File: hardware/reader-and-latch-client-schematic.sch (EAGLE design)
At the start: 23 parts, among them IC1 MAX3468ESA, IC2 L272M, T1 TIP32

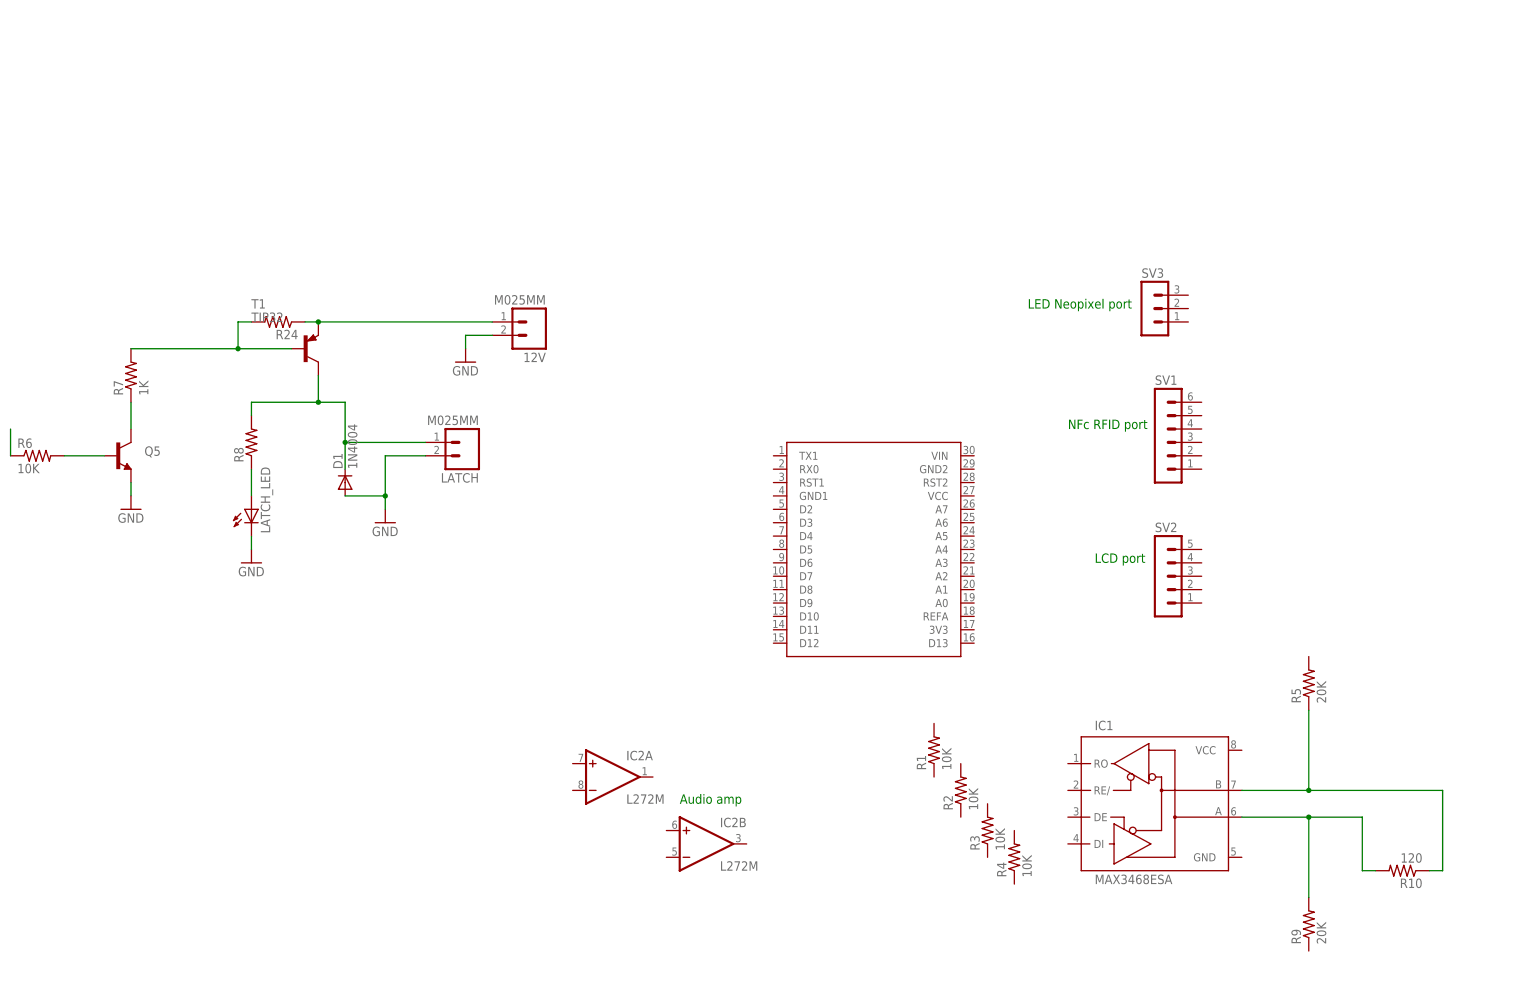
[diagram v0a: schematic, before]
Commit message: Add Tom's 13-2015 schematic
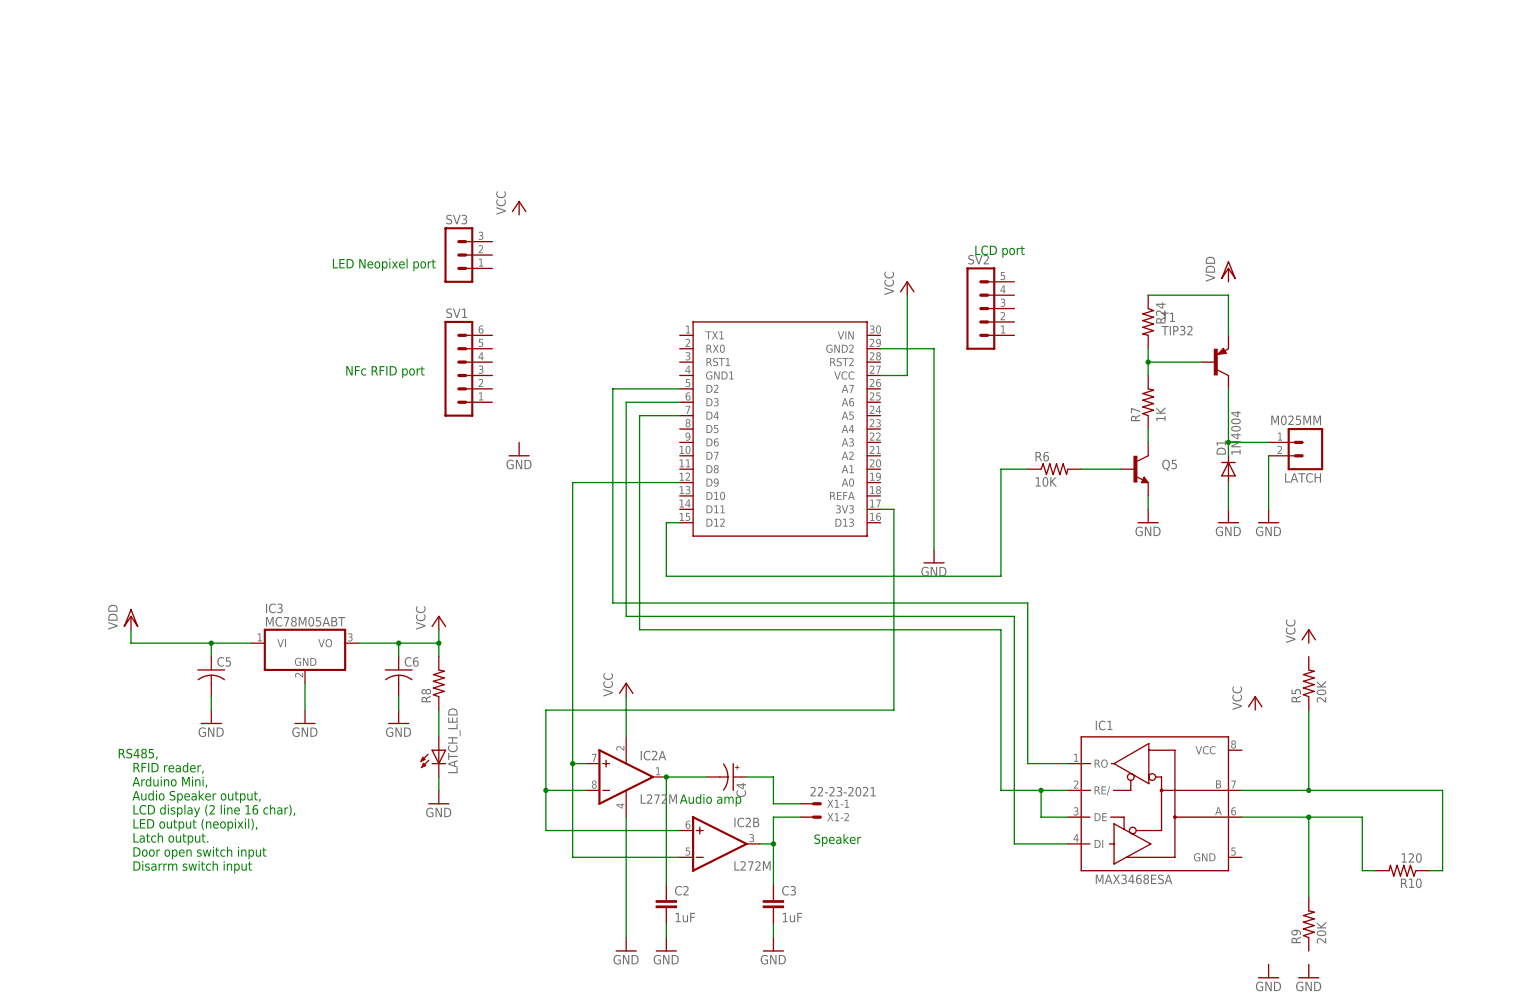
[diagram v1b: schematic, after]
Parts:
- removed 12V: M025MM, SparkFun-Connectors:M025MM
- removed R1, R2, R3, R4: 10K, SparkFun-Resistors:10KOHM1/6W5%(PTH)KIT
- added C2, C3: 1uF, SparkFun-Capacitors:1UF-25V-10%(0805)
- added C4: (no value), SparkFun-Capacitors:CAP_POLPTH1
- added C5, C6: (no value), rcl:C-USC1206
- added IC3: MC78M05ABT, linear:MC78M05ABT
- added X1: 22-23-2021, con-molex:22-23-2021
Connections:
- removed net N$28: R6.1
- new net N$13: IC1.DI, U$1.D3
- new net N$14: IC1.DE, IC1.RE/, U$1.D4
- new net N$16: R6.1, U$1.D12
- new net N$2: IC2A.-IN, IC2B.+IN, U$1.3V3
- new net N$5: IC2A.+IN, IC2B.-IN, U$1.D9
- new net N$6: IC1.RO, U$1.D2
- new net N$7: C2.1, C4.-, IC2A.OUT
- new net N$8: C4.+, X1-1.S
- new net N$9: C3.1, IC2B.OUT, X1-2.S
- new net VCC: C6.1, IC2P.V+, IC3.VO, R8.2, U$1.VCC
- new net VDD: C5.1, IC3.VI
- net GND: now also C2.2, C3.2, C5.2, C6.2, IC2P.GND, IC3.GND, U$1.GND2; no longer 12V.2
- net N$17: no longer 12V.1
- net N$29: no longer R8.2
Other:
- note added: "RS485, RFID reader, Arduino Mini, Audio Speaker output, LCD display (2 line 16 char), LED output (neopixil), Latch output. Door open switch input Disarrm switch input"
- note added: "Speaker"
- moved on the sheet: D1, IC2A, IC2B, LATCH, LATCH_LED, Q5, R24, R6, R7, R8, SV1, SV2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

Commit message: Update from 9-2015
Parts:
- removed SV2: (no value), con-lstb:MA05-1
- added JP1: (no value), pinhead:PINHD-1X16
- added LATCH1: M025MM, SparkFun-Connectors:M025MM
- added Q1, Q2: (no value), SparkFun-DiscreteSemi:TRANSISTOR_NPNTO-92-AMMO
- added R1: (no value), pot:TRIM_EU-CT6
- added R11, R12, R13, R14, R3, R4: 1K, SparkFun-Resistors:10KOHM1/6W5%(PTH)KIT
- added R2: 220, SparkFun-Resistors:10KOHM1/6W5%(PTH)KIT
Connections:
- new net N$1: JP1.3, R1.S
- new net N$18: SV3.2, U$1.D10
- new net N$19: JP1.4, U$1.D12
- new net N$20: JP1.6, U$1.D11
- new net N$21: SV1.6, U$1.D5
- new net N$22: SV1.5, U$1.D4
- new net N$23: SV1.4, U$1.D3
- new net N$24: SV1.3, U$1.D2
- new net N$25: JP1.15, R2.2
- new net N$26: JP1.14, U$1.A7
- new net N$27: JP1.13, U$1.A6
- new net N$28: JP1.12, U$1.A5
- new net N$30: JP1.11, U$1.A4
- new net N$31: Q1.B, R3.2, R4.1
- new net N$32: Q2.C, U$1.A3
- new net N$33: Q1.C, U$1.A2
- net GND: now also IC1.GND, JP1.1, JP1.16, JP1.5, Q1.E, Q2.E, R1.A, R12.1, R3.1, R9.1, SV1.1, SV3.1
- net N$13: now also U$1.D7; no longer U$1.D3
- net N$14: now also U$1.D8; no longer U$1.D4
- net N$16: now also U$1.D13; no longer U$1.D12
- net N$17: now also Q2.B, R12.2, R13.1; no longer R24.1, T1.E
- net N$3: now also LATCH1.2
- net N$4: now also LATCH1.1
- net N$6: now also U$1.D6; no longer U$1.D2
- net VCC: now also IC1.VCC, JP1.2, R1.E, R11.2, R14.2, R2.1, R5.2, SV1.2, SV3.3
- net VDD: now also R24.1, T1.E
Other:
- note added: "5 volt regulator"
- note added: "Alarm set button"
- note added: "Door Open"
- note added: "Features list RS485, RFID reader, Arduino Mini, Audio Speaker output, LCD display (2 line 16 char), LED output (neopixil), Latch output. Door open switch input Disarrm switch input"
- note added: "RS485 data"
- note removed: "RS485, RFID reader, Arduino Mini, Audio Speaker output, LCD display (2 line 16 char), LED output (neopixil), Latch output. Door open switch input Disarrm switch input"
- moved on the sheet: D1, LATCH, Q5, R24, R6, R7, SV1, T1
